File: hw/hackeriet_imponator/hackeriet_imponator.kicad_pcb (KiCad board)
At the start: 2 copper layers, 142.7 x 133 mm, 46 parts, among them J1 USB4085-GF-A, J10 AAA -, J11 AAA -, J2 UPDI Programming, J3 External Battery Connector, J4 Shitty Add On, J5 Unused pins, J6 AAA +, J7 AAA +, J8 AAA +, J9 AAA -, U1 ATtiny804-SS, U2 MCP2221AxSL

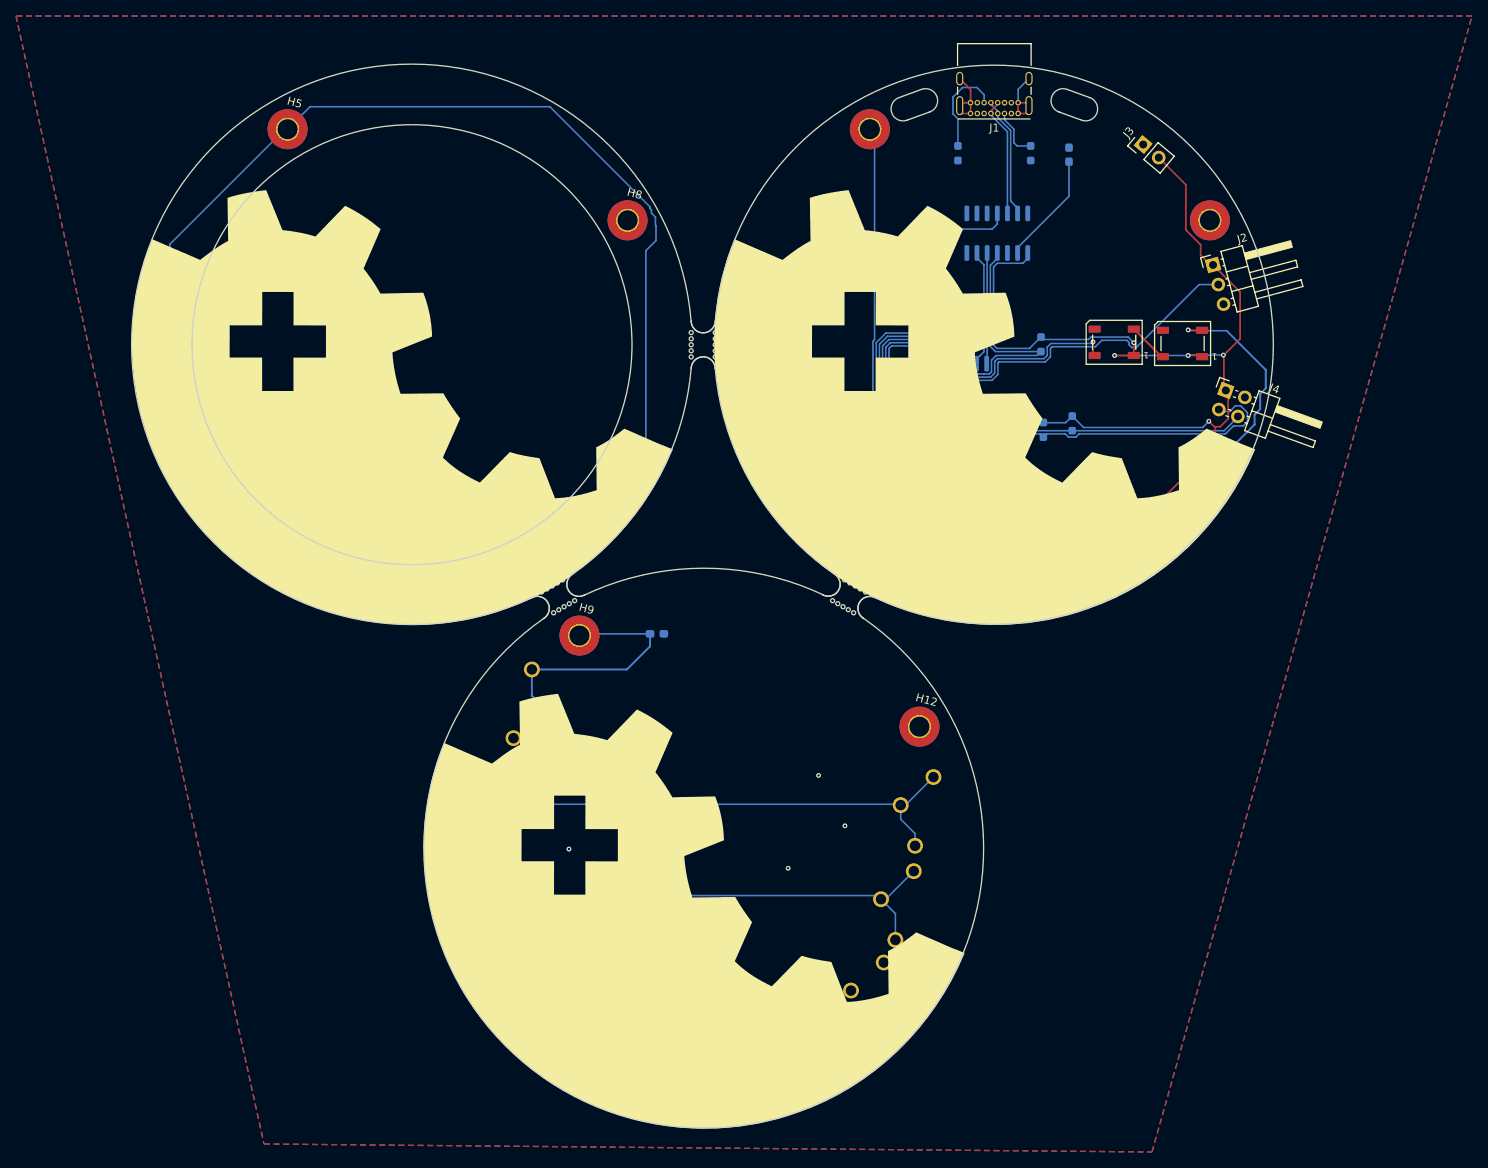
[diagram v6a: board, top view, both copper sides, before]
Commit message: Removed outer ring and battery backplate. Ready to apply TODOs
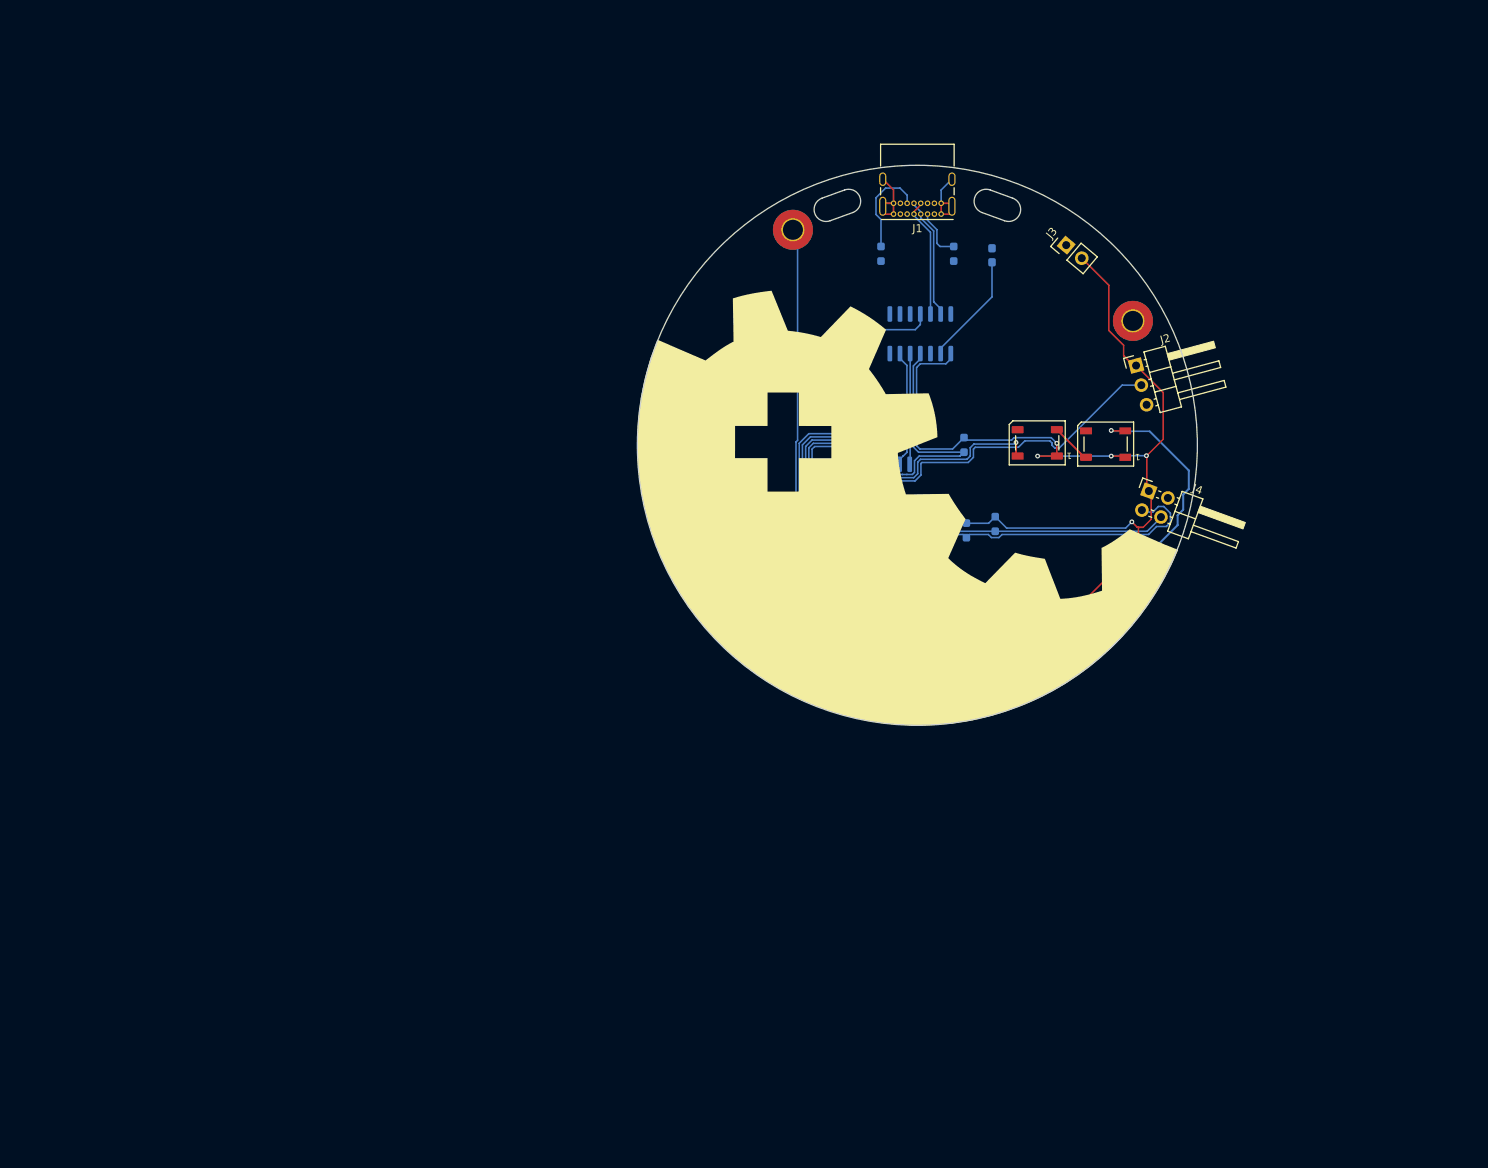
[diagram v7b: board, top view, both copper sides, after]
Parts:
- removed C3: 22uF, Capacitor_SMD:C_0603_1608Metric_Pad1.08x0.95mm_HandSolder
- removed D4, D5: WS2812B, LED_SMD:LED_WS2812B_PLCC4_5.0x5.0mm_P3.2mm
- removed H10, H11, H12, H5, H6, H7, H8, H9: MountingHole_Pad, MountingHole:MountingHole_2.5mm_Pad_TopBottom
- removed J10, J11, J9: AAA -, imponator_footprint_lib:BAT_591
- removed J6, J7, J8: AAA +, imponator_footprint_lib:BAT_597
- removed the REF** at (106.3, 141.3)
- removed the REF** at (108.8, 129.5)
- removed the REF** at (102.6, 152.7)
- removed mouse-bite-3mm-slot (x3): VAL**, imponator_footprint_lib:mouse-bite-3mm-slot
- moved C2 15.8 mm to (125.2, 77.1)
- moved D2 15.8 mm to (148.7, 90.4)
- moved H1 15.8 mm to (118.1, 63.7)
- moved R3 15.8 mm to (139.5, 90.6)
- moved R4 15.8 mm to (139.8, 101.3)
- moved R5 15.8 mm to (143.4, 100.5)
- moved U1 15.8 mm to (128.9, 95.5)
- moved D1 15.8 mm to (143.0, 66.9)
- moved R1 15.8 mm to (138.2, 66.7)
- moved R2 15.8 mm to (129.1, 66.7)
- moved C1 15.8 mm to (122.0, 95.6)
- moved H3 15.8 mm to (106.7, 106.2)
- moved J5 15.8 mm to (123.6, 119.1)
- moved H2 15.8 mm to (149.2, 117.6)
- moved D3 15.8 mm to (157.2, 90.5)
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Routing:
- net BATT: track 453.9 -> 258.1 mm
- net Net-(J10-Pin_1): track 71.0 -> 0.00 mm
- net Net-(J7-Pin_1): track 69.6 -> 0.00 mm
- net Net-(D4-DOUT): track 48.1 -> 0.00 mm
- net Net-(D4-DIN): track 15.5 -> 0.00 mm
- net GND: vias 13 -> 0
- removed copper zone on B.Cu, net GND
- removed copper zone on F.Cu, net GND
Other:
- board size 142.7 x 133 mm -> 70 x 70 mm
- board text added: "${REFERENCE}"

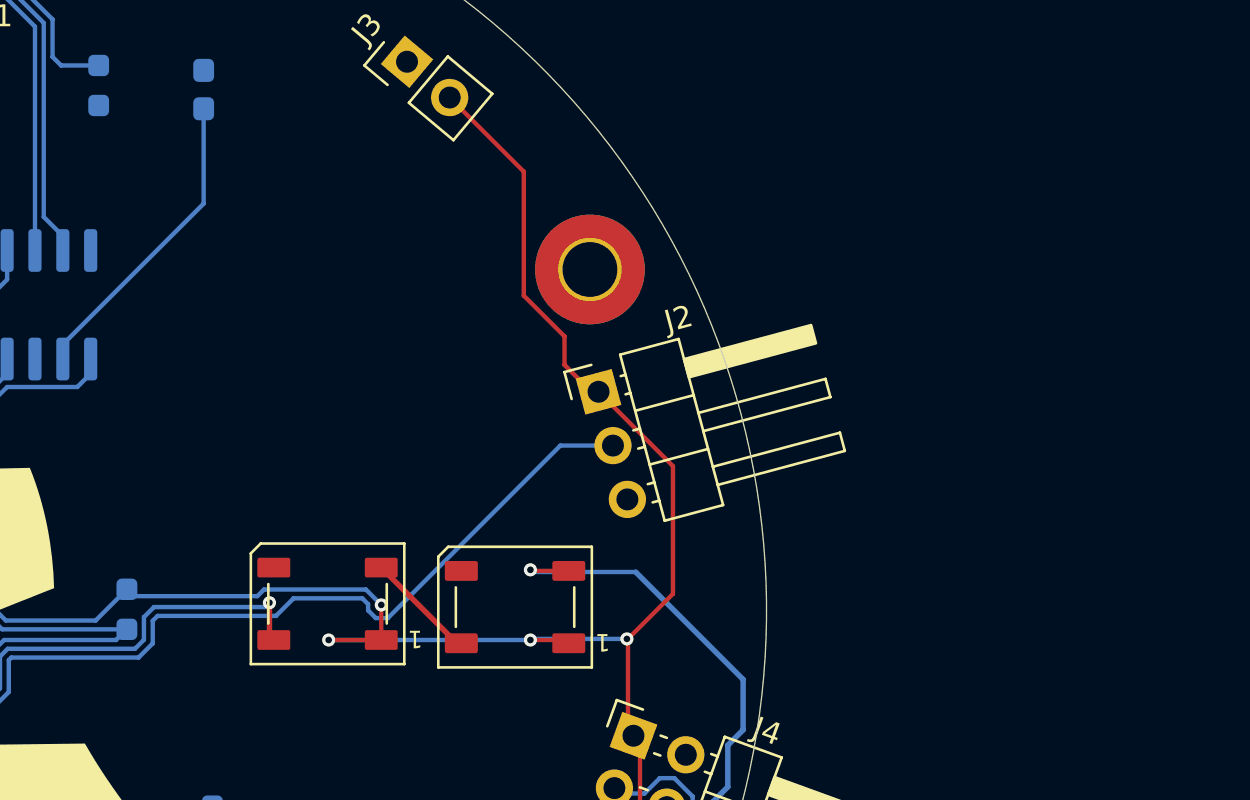
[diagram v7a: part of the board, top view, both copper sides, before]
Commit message: Added switch between batt and USB. Changed LEDs to sideways
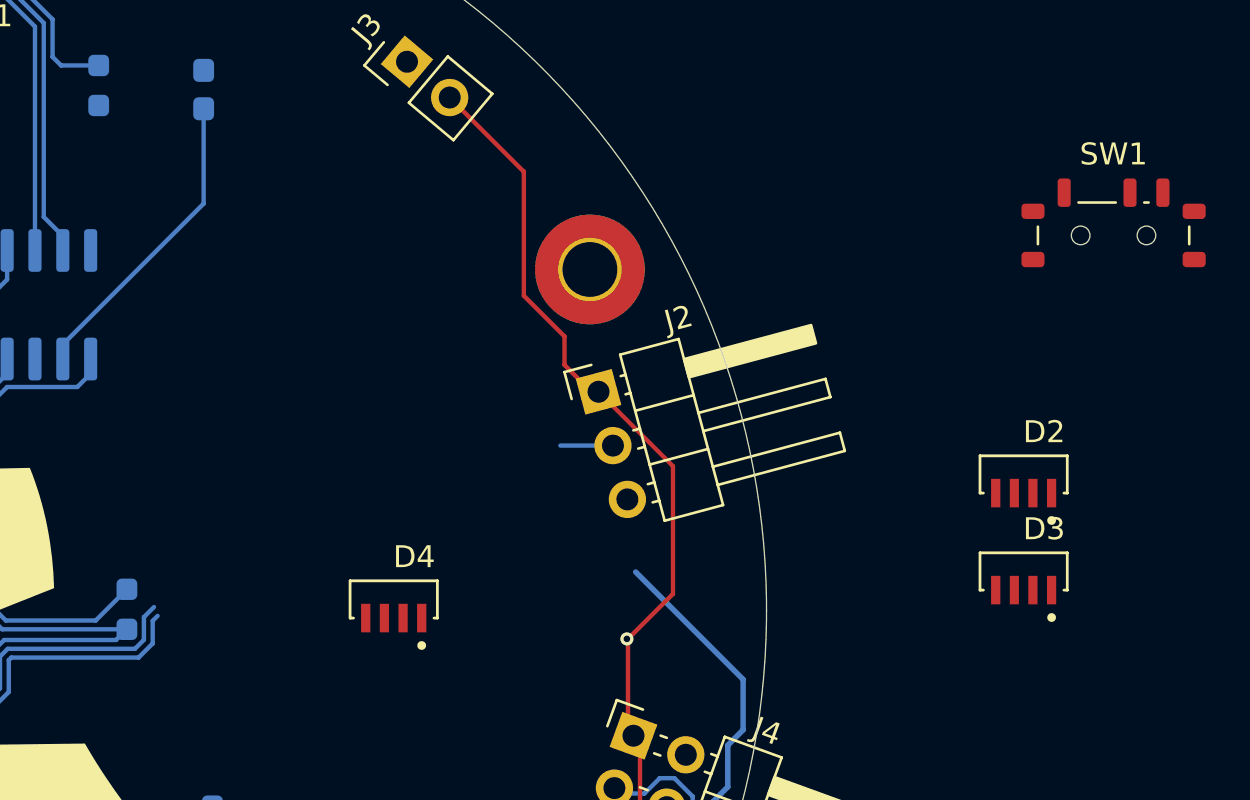
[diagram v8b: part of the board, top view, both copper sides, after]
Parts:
- added D4: WS2812B, imponator_footprint_lib:LED_WS2812B-4020, F.Cu at (151.7, 90.2)
- added SW1: SW_SPDT, Button_Switch_SMD:SW_SPDT_Shouhan_MSK12C02, F.Cu at (184.5, 73.6)
- D2, D3: footprint LED_SMD:LED_WS2812B_PLCC4_5.0x5.0mm_P3.2mm -> imponator_footprint_lib:LED_WS2812B-4020
- moved D2 32.3 mm to (180.4, 84.5), turned to 0 degrees
- moved D3 23.2 mm to (180.4, 88.9), turned to 0 degrees
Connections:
- C1 pad 2: BATT -> VDD
- D2 pad 1: BATT -> VDD
- D3 pad 1: BATT -> VDD
- D3 pad 2: RGB DOUT, to top PCB -> Net-(D3-DOUT)
- J1 pad A4: unconnected-(J1-VBUS-PadA4)_2 -> USB_VDD
- J1 pad A9: unconnected-(J1-VBUS-PadA4)_1 -> USB_VDD
- J1 pad B4: unconnected-(J1-VBUS-PadA4) -> USB_VDD
- J1 pad B9: unconnected-(J1-VBUS-PadA4)_3 -> USB_VDD
- J2 pad 1: BATT -> VDD
- J4 pad 1: BATT -> VDD
- J5 pad 1: PA3 -> unconnected-(J5-Pin_1-Pad1)
- J5 pad 2: PA4 -> unconnected-(J5-Pin_2-Pad2)
- J5 pad 3: PA5 -> unconnected-(J5-Pin_3-Pad3)
- J5 pad 4: PA6 -> unconnected-(J5-Pin_4-Pad4)
- J5 pad 5: PA7 -> unconnected-(J5-Pin_5-Pad5)
- R3 pad 1: BATT -> VDD
- R4 pad 1: BATT -> VDD
- R5 pad 1: BATT -> VDD
- U1 pad 1: BATT -> VDD
- U2 pad 1: BATT -> VDD
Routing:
- net BATT: track 258.1 -> 204.5 mm, vias 7 -> 4
- net Net-(J2-Pin_2): track 40.8 -> 18.3 mm
- net VDD: track 0.00 -> 22.3 mm
- net WS2812B LED RGB Control: track 24.0 -> 16.8 mm, vias 1 -> 0
- net RGB DOUT, to top PCB: track 45.0 -> 38.3 mm, vias 1 -> 0
- net Net-(D2-DOUT): track 5.08 -> 0.00 mm
